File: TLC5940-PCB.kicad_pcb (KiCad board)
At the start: 2 copper layers, 29.2 x 20.3 mm, 7 parts, among them J3 Conn_02x08_Counter_Clockwise, J4 Conn_01x03_Male, U1 TLC5940PWP

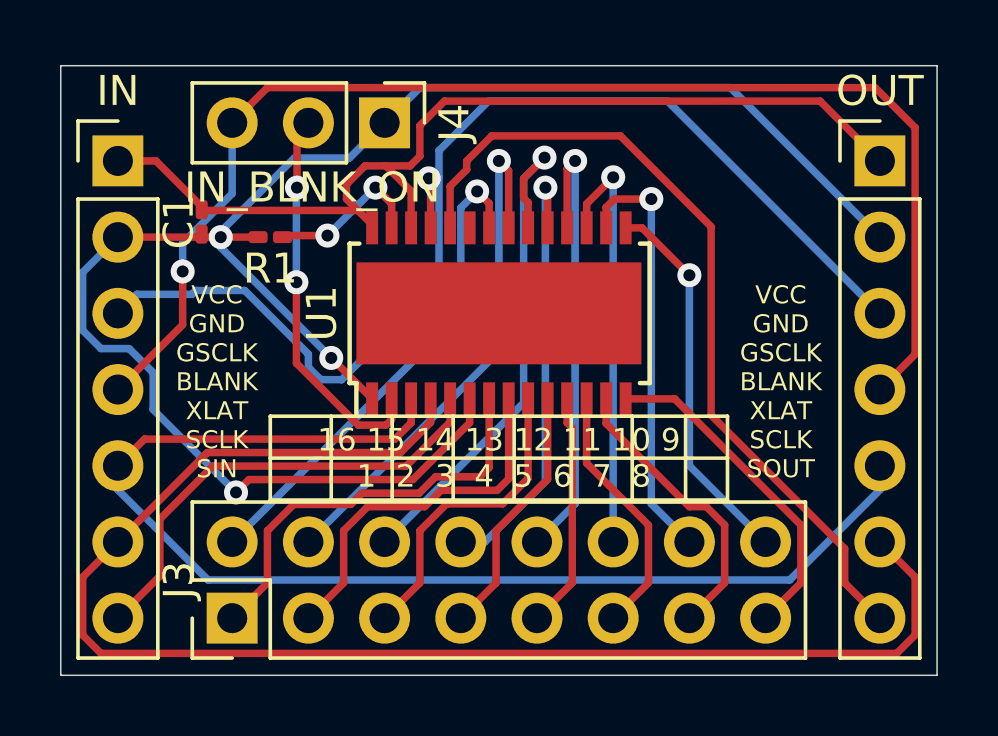
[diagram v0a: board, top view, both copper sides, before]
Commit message: Update resistor/capacitor footprints
These were 0201_0603 instead of 0603_1608.
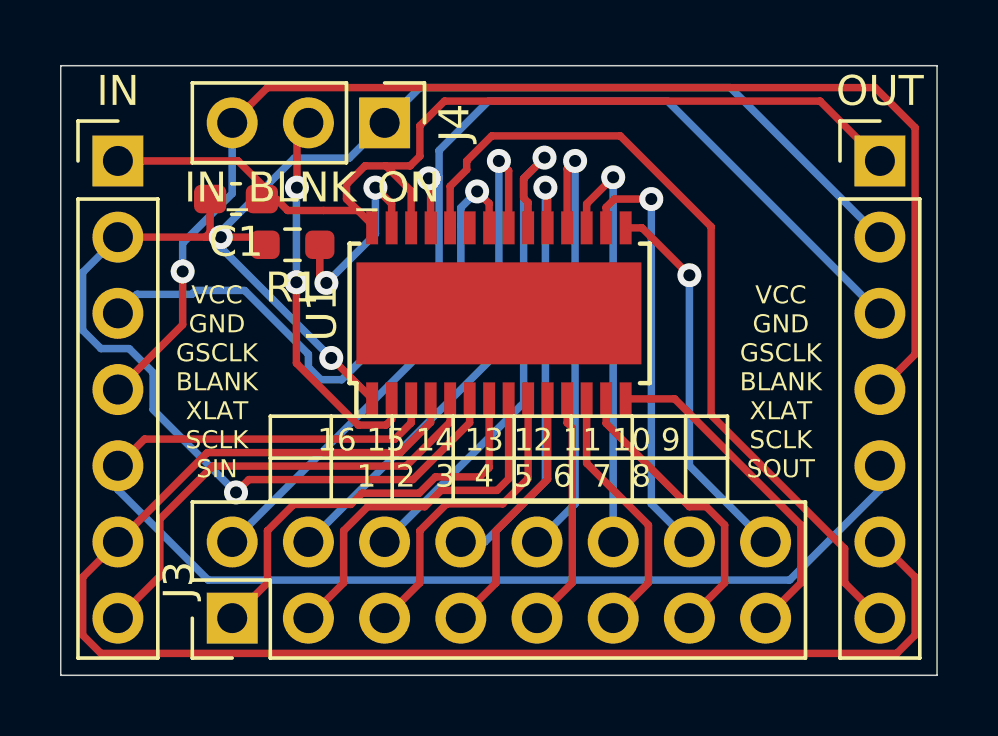
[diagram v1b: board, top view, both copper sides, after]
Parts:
- C1: footprint Capacitor_SMD:C_0201_0603Metric_Pad0.64x0.40mm_HandSolder -> Capacitor_SMD:C_0603_1608Metric_Pad1.08x0.95mm_HandSolder
- R1: footprint Resistor_SMD:R_0201_0603Metric_Pad0.64x0.40mm_HandSolder -> Resistor_SMD:R_0603_1608Metric_Pad0.98x0.95mm_HandSolder
- moved C1 1.37 mm to (146.2, 110.5), turned to 180 degrees
- moved R1 0.78 mm to (148.1, 112.0)
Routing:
- net GND: track 59.6 -> 61.3 mm
- net Net-(R1-Pad1): track 5.35 -> 6.78 mm
- net VCC: track 33.3 -> 33.8 mm

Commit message: Move traces around + add ground plane
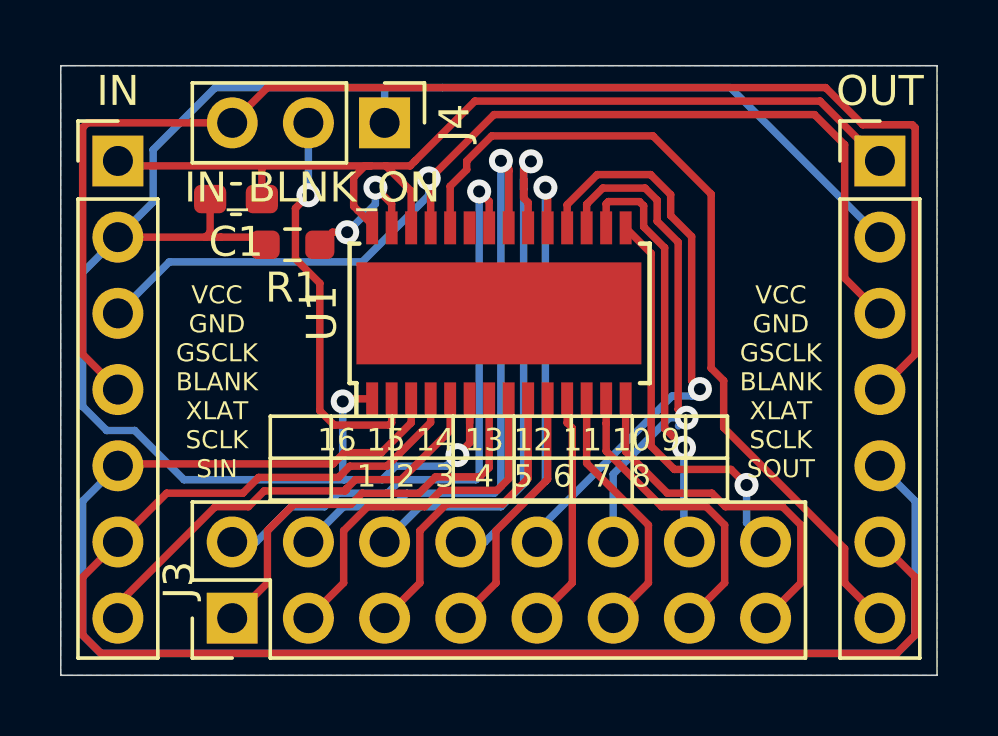
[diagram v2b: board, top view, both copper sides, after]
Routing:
- net Net-(IN1-Pad5): track 40.7 -> 51.7 mm
- net Net-(J3-Pad15): track 17.7 -> 22.7 mm
- net Net-(J3-Pad12): track 15.6 -> 19.5 mm
- net Net-(IN1-Pad4): track 43.5 -> 47.3 mm, vias 1 -> 0
- net Net-(J3-Pad16): track 16.4 -> 20.0 mm
- net GND: track 61.3 -> 64.5 mm, vias 3 -> 2
- net Net-(J3-Pad11): track 14.2 -> 17.1 mm
- net Net-(IN1-Pad3): track 38.6 -> 36.1 mm
- net Net-(R1-Pad1): track 6.78 -> 4.53 mm
- net Net-(J3-Pad14): track 17.7 -> 19.7 mm
- net Net-(J3-Pad9): track 12.7 -> 14.1 mm
- net Net-(J3-Pad8): track 11.2 -> 12.2 mm
- net Net-(IN1-Pad7): track 15.7 -> 15.0 mm
- net Net-(OUT1-Pad7): track 27.6 -> 28.2 mm
- net Net-(J4-Pad2): track 13.0 -> 13.5 mm, vias 2 -> 1
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- added copper zone on B.Cu, net GND

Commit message: Move cap closer to TLC VCC + Decrease via size
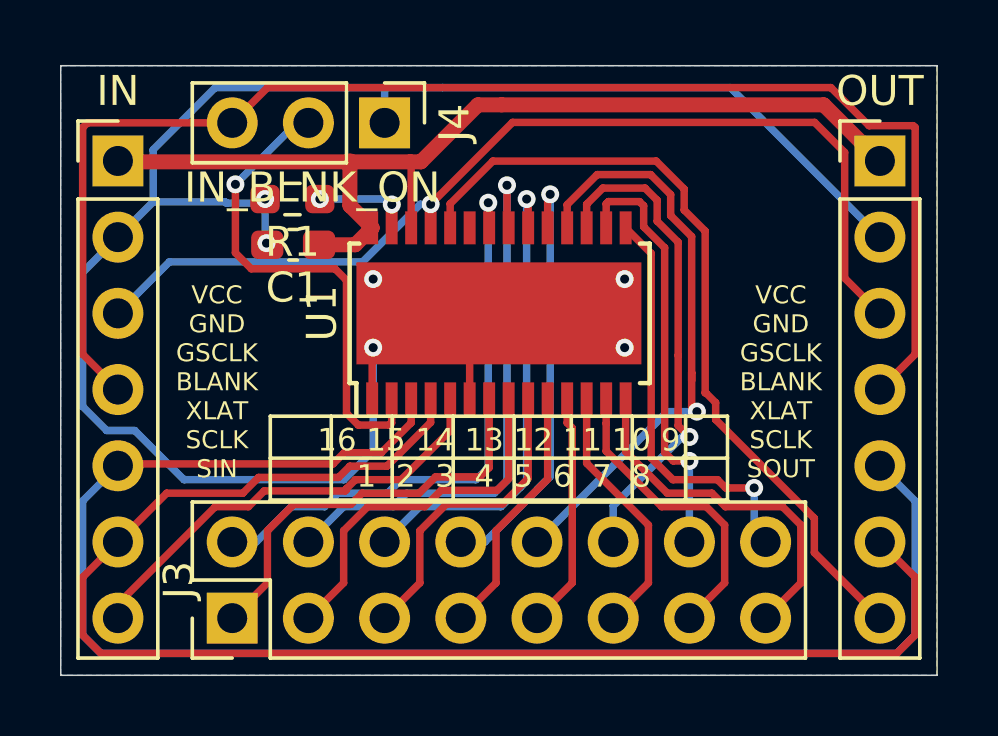
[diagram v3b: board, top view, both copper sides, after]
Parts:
- moved C1 2.44 mm to (148.1, 112.0)
- moved R1 1.52 mm to (148.1, 110.5)
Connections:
- U1 pad 29: Net-(U1-Pad29) -> GND
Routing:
- net Net-(J3-Pad15): track 22.7 -> 18.8 mm
- net Net-(J3-Pad14): track 19.7 -> 16.0 mm
- net Net-(J4-Pad2): track 13.5 -> 16.6 mm
- net Net-(IN1-Pad3): track 36.1 -> 33.9 mm
- net Net-(OUT1-Pad7): track 28.2 -> 26.6 mm
- net GND: track 64.5 -> 63.3 mm, vias 2 -> 6
- net Net-(R1-Pad1): track 4.53 -> 3.33 mm
- net VCC: track 33.4 -> 34.2 mm
- net Net-(J3-Pad16): track 20.0 -> 19.2 mm
